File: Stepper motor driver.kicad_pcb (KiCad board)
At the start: 2 copper layers, 22 parts, among them Q1 TIP120, Q2 TIP120, Q3 TIP120, Q4 TIP120, U1 74LS175, U2 74LS157

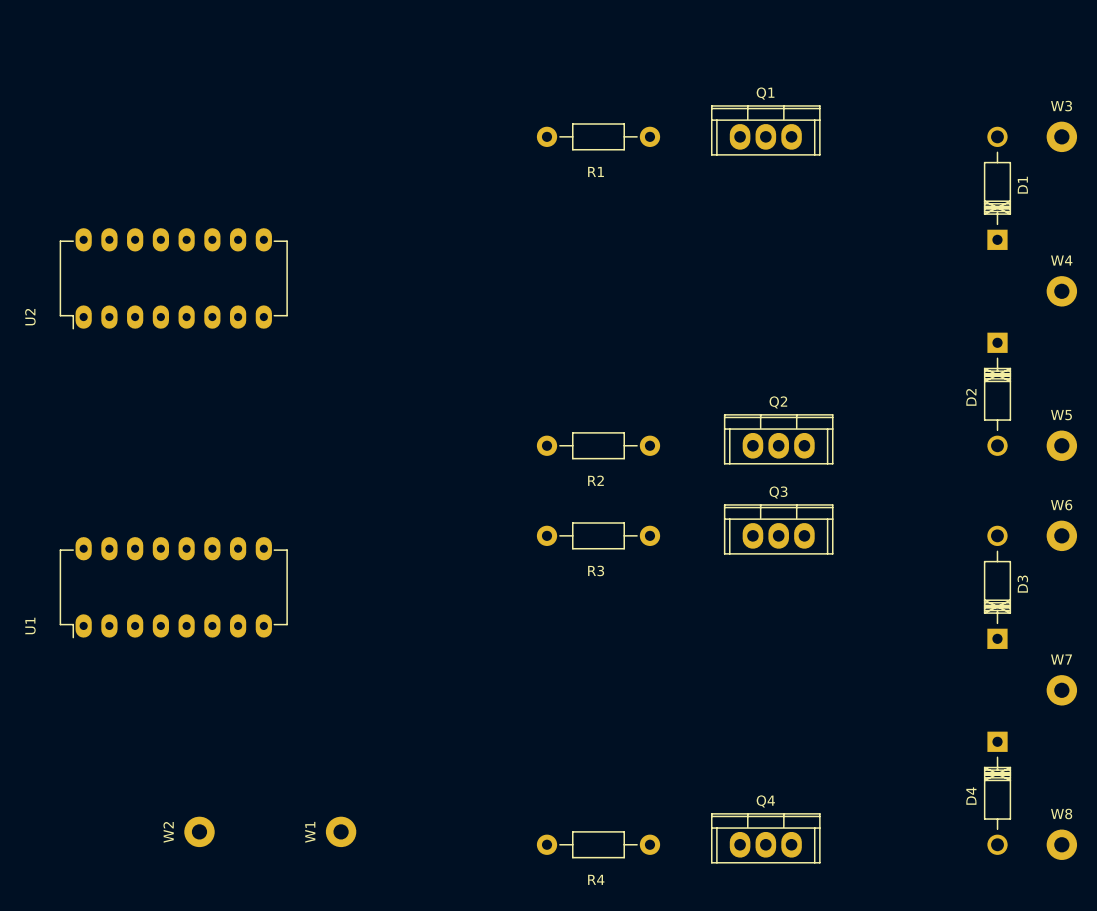
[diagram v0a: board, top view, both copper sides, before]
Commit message: finished PCB initial routing
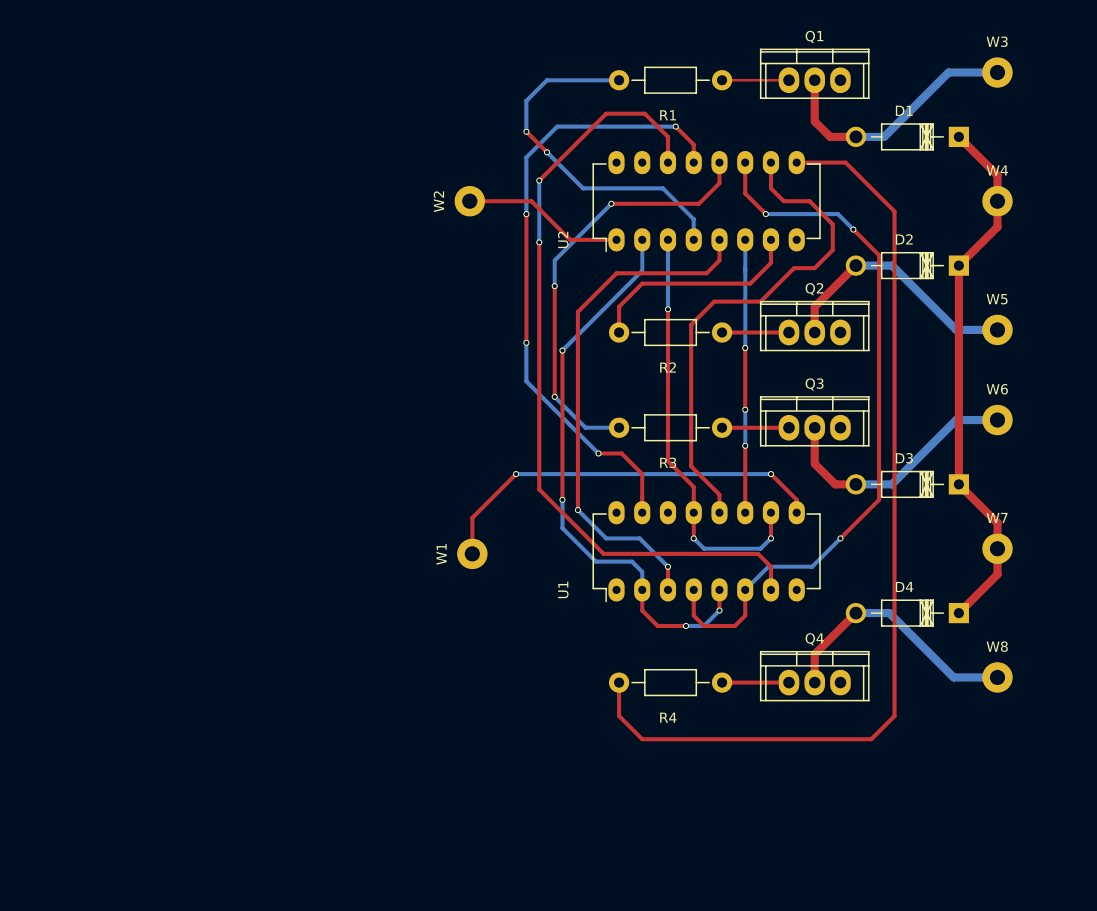
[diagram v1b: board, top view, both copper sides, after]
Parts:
- moved W2 67.7 mm to (203.2, 38.1)
- moved U2 53.1 mm to (217.7, 41.9)
- moved U1 52.7 mm to (217.7, 76.5)
- moved W1 30.3 mm to (203.5, 72.9)
- moved W8 17.7 mm to (255.3, 85.1)
- moved R4 17.5 mm to (228.1, 85.6)
- moved Q4 16.7 mm to (237.2, 85.6)
- moved D3 15.7 mm to (251.5, 66.0), turned to 180 degrees
- moved W7 15.3 mm to (255.3, 72.4)
- moved D4 13.3 mm to (251.5, 78.7), turned to 180 degrees
- moved R2 13.2 mm to (228.1, 51.1)
- moved W6 13.1 mm to (255.3, 59.7)
- moved W5 13.1 mm to (255.3, 50.8)
- moved R3 12.8 mm to (228.1, 60.5)
- moved Q2 11.7 mm to (237.2, 51.1)
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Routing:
- net Net-(R4-Pad2): track 0.00 -> 93.8 mm
- net /A1-: track 0.00 -> 77.7 mm, vias 0 -> 2
- net /A1+: track 0.00 -> 70.8 mm, vias 0 -> 3
- net /B2+: track 0.00 -> 61.4 mm, vias 0 -> 4
- net /B1+: track 0.00 -> 56.1 mm, vias 0 -> 4
- net +5V: track 0.02 -> 53.3 mm
- net /B1-: track 0.00 -> 51.2 mm, vias 0 -> 2
- net /B2-: track 0.00 -> 49.4 mm
- net Net-(R3-Pad2): track 0.00 -> 42.5 mm, vias 0 -> 3
- net /A2-: track 0.00 -> 41.5 mm, vias 0 -> 3
- net /CLK: track 0.00 -> 39.7 mm, vias 0 -> 2
- net Net-(R1-Pad2): track 0.00 -> 35.2 mm, vias 0 -> 2
- net /A2+: track 0.00 -> 27.2 mm, vias 0 -> 3
- net Net-(D1-Pad2): track 0.00 -> 25.4 mm
- net Net-(D4-Pad2): track 0.00 -> 25.1 mm
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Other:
- net class high current wire added: clearance 0.2, trace_width 0.8, via_dia 0.6, via_drill 0.4
- net class thicker wire added: clearance 0.2, trace_width 0.4, via_dia 0.6, via_drill 0.4

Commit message: fixed schematic and finished all routing
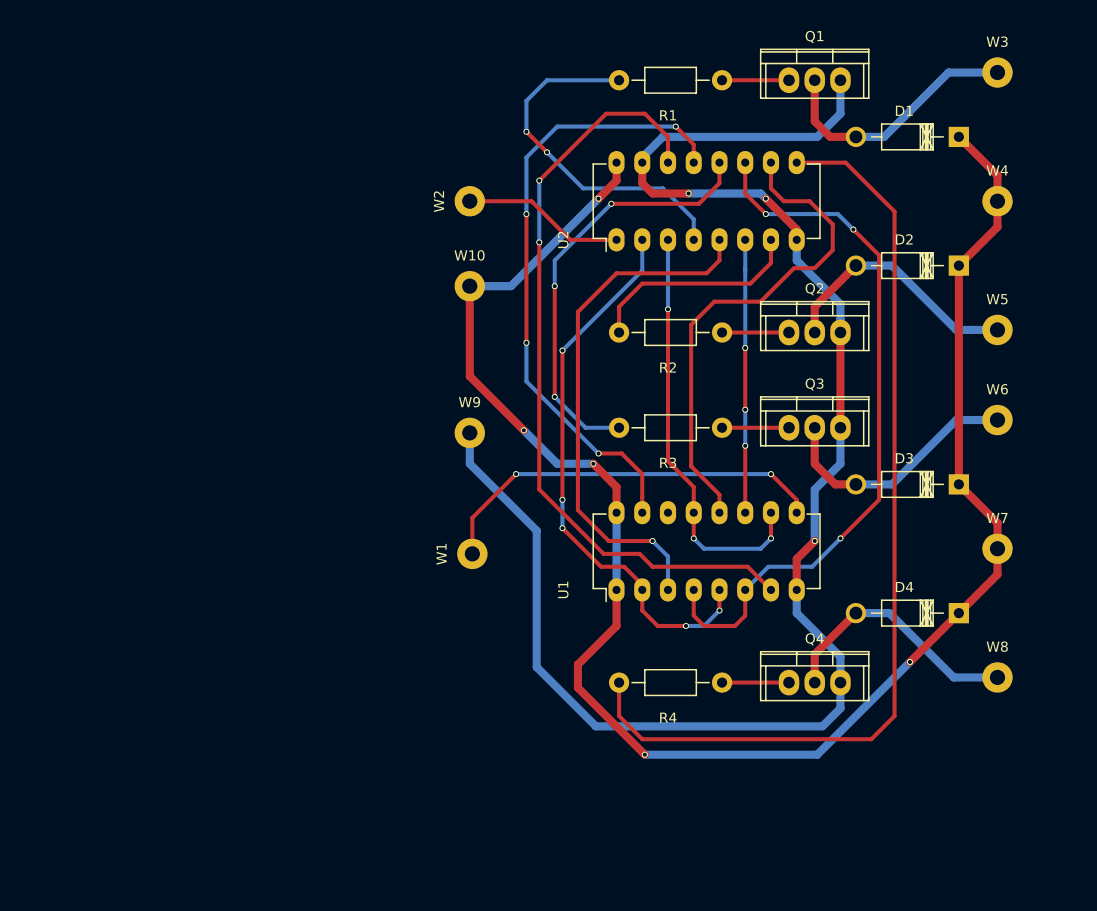
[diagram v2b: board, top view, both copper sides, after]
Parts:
- added W10: TEST_1P, Measurement_Points:Measurement_Point_Round-TH_Big, F.Cu at (203.2, 46.5)
- added W9: TEST_1P, Measurement_Points:Measurement_Point_Round-TH_Big, F.Cu at (203.2, 61.0)
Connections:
- D1 pad 1: +5V -> VCC
- D2 pad 1: +5V -> VCC
- D3 pad 1: +5V -> VCC
- D4 pad 1: +5V -> VCC
- U1 pad 1: +5V -> VCC
- W4 pad 1: +5V -> VCC
- W7 pad 1: +5V -> VCC
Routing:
- net VCC: track 0.00 -> 169.3 mm, vias 0 -> 5
- net GND: track 0.00 -> 155.9 mm, vias 0 -> 3
- net +5V: track 53.3 -> 0.00 mm
- net /A1-: track 77.7 -> 76.4 mm
- net /B1+: track 56.1 -> 55.4 mm, vias 4 -> 5
- net /B1-: track 51.2 -> 51.7 mm, vias 2 -> 1

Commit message: finished PCB completely, added gerber files and picture of layout
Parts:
- Coil 1+: renamed from W3
- Coil 1-: renamed from W5
- Coil 2+: renamed from W6
- Coil 2-: renamed from W8
- renumbered W1 to CLK, W2 to DIR, W9 to GND, W4 to VCC, W7 to VCC, W10 to VCC
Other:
- board outline added: 63 x 74.4 mm
- board text added: "Jake Vidal"
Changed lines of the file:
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@@
     (links 46)
     (no_connects 1)
-    (area 0 0 0 0)
+    (area 196.520999 20.244999 259.663001 94.817001)
     (thickness 1.6)
-    (drawings 0)
+    (drawings 7)
     (tracks 252)
     (zones 0)
@@
     (visible_elements 7FFFFFFF)
     (pcbplotparams
-      (layerselection 0x00030_80000001)
+      (layerselection 0x010f0_80000001)
       (usegerberextensions false)
-      (excludeedgelayer true)
+      (excludeedgelayer false)
       (linewidth 0.100000)
       (plotframeref false)
@@
       (psa4output false)
       (plotreference true)
-      (plotvalue true)
+      (plotvalue false)
       (plotinvisibletext false)
-      (padsonsilk false)
+      (padsonsilk true)
       (subtractmaskfromsilk false)
       (outputformat 1)
       (mirror false)
-      (drillshape 1)
+      (drillshape 0)
       (scaleselection 1)
-      (outputdirectory ""))
+      (outputdirectory ../../../))
   )
   (net 0 "")
@@
     (descr "Diode, DO-41, SOD81, Horizontal, RM 10mm,")
     (tags "Diode, DO-41, SOD81, Horizontal, RM 10mm, 1N4007, SB140,")
-    (fp_text reference D1 (at 5.38734 2.53746 180) (layer F.SilkS)
-      (effects (font (size 1 1) (thickness 0.15)))
-    )
-    (fp_text value 1N4003 (at 4.37134 -3.55854 180) (layer F.Fab)
+    (fp_text reference D1 (at 4.318 -2.286 180) (layer F.SilkS)
+      (effects (font (size 1 1) (thickness 0.15)))
+    )
+    (fp_text value 1N4003 (at 4.826 2.794 180) (layer F.Fab)
       (effects (font (size 1 1) (thickness 0.15)))
     )
@@
     (descr "Diode, DO-41, SOD81, Horizontal, RM 10mm,")
     (tags "Diode, DO-41, SOD81, Horizontal, RM 10mm, 1N4007, SB140,")
-    (fp_text reference D2 (at 5.38734 2.53746 180) (layer F.SilkS)
+    (fp_text reference D2 (at 4.318 2.286 180) (layer F.SilkS)
       (effects (font (size 1 1) (thickness 0.15)))
     )
@@
     (descr "Diode, DO-41, SOD81, Horizontal, RM 10mm,")
     (tags "Diode, DO-41, SOD81, Horizontal, RM 10mm, 1N4007, SB140,")
-    (fp_text reference D3 (at 5.38734 2.53746 180) (layer F.SilkS)
-      (effects (font (size 1 1) (thickness 0.15)))
-    )
-    (fp_text value 1N4003 (at 4.37134 -3.55854 180) (layer F.Fab)
+    (fp_text reference D3 (at 4.572 -2.286 180) (layer F.SilkS)
+      (effects (font (size 1 1) (thickness 0.15)))
+    )
+    (fp_text value 1N4003 (at 5.08 2.794 180) (layer F.Fab)
       (effects (font (size 1 1) (thickness 0.15)))
     )
@@
     (descr "Diode, DO-41, SOD81, Horizontal, RM 10mm,")
     (tags "Diode, DO-41, SOD81, Horizontal, RM 10mm, 1N4007, SB140,")
-    (fp_text reference D4 (at 5.38734 2.53746 180) (layer F.SilkS)
+    (fp_text reference D4 (at 4.572 2.286 180) (layer F.SilkS)
       (effects (font (size 1 1) (thickness 0.15)))
     )
@@
     (descr "Non Isolated JEDEC TO-220 Package")
     (tags "Power Integration YN Package")
-    (fp_text reference Q1 (at 0 -4.318) (layer F.SilkS)
+    (fp_text reference Q1 (at -4.318 2.794) (layer F.SilkS)
       (effects (font (size 1 1) (thickness 0.15)))
     )
@@
     (descr "Non Isolated JEDEC TO-220 Package")
     (tags "Power Integration YN Package")
-    (fp_text reference Q2 (at 0 -4.318) (layer F.SilkS)
+    (fp_text reference Q2 (at -3.81 2.794) (layer F.SilkS)
       (effects (font (size 1 1) (thickness 0.15)))
     )
@@
     (descr "Non Isolated JEDEC TO-220 Package")
     (tags "Power Integration YN Package")
-    (fp_text reference Q3 (at 0 -4.318) (layer F.SilkS)
+    (fp_text reference Q3 (at -3.81 -4.318) (layer F.SilkS)
       (effects (font (size 1 1) (thickness 0.15)))
     )
@@
     (descr "Non Isolated JEDEC TO-220 Package")
     (tags "Power Integration YN Package")
-    (fp_text reference Q4 (at 0 -4.318) (layer F.SilkS)
+    (fp_text reference Q4 (at -4.064 -4.318) (layer F.SilkS)
       (effects (font (size 1 1) (thickness 0.15)))
     )
@@
     (descr "Resistor, Axial,  RM 10mm, 1/3W")
     (tags "Resistor Axial RM 10mm 1/3W")
-    (fp_text reference R1 (at 5.32892 -3.50012 180) (layer F.SilkS)
+    (fp_text reference R1 (at 6.858 -2.54 180) (layer F.SilkS)
       (effects (font (size 1 1) (thickness 0.15)))
     )
@@
     (descr "Resistor, Axial,  RM 10mm, 1/3W")
     (tags "Resistor Axial RM 10mm 1/3W")
-    (fp_text reference R2 (at 5.32892 -3.50012 180) (layer F.SilkS)
+    (fp_text reference R2 (at 6.858 -2.794 180) (layer F.SilkS)
       (effects (font (size 1 1) (thickness 0.15)))
     )
@@
     (descr "Resistor, Axial,  RM 10mm, 1/3W")
     (tags "Resistor Axial RM 10mm 1/3W")
-    (fp_text reference R3 (at 5.32892 -3.50012 180) (layer F.SilkS)
+    (fp_text reference R3 (at 6.858 -2.794 180) (layer F.SilkS)
       (effects (font (size 1 1) (thickness 0.15)))
     )
@@
     (descr "Resistor, Axial,  RM 10mm, 1/3W")
     (tags "Resistor Axial RM 10mm 1/3W")
-    (fp_text reference R4 (at 5.32892 -3.50012 180) (layer F.SilkS)
-      (effects (font (size 1 1) (thickness 0.15)))
-    )
-    (fp_text value 180 (at 5.08 3.81 180) (layer F.Fab)
+    (fp_text reference R4 (at 6.858 -2.794 180) (layer F.SilkS)
+      (effects (font (size 1 1) (thickness 0.15)))
+    )
+    (fp_text value 180 (at 5.334 2.54 180) (layer F.Fab)
       (effects (font (size 1 1) (thickness 0.15)))
     )
@@
     (descr "16-lead dip package, row spacing 7.62 mm (300 mils), longer pads")
     (tags "dil dip 2.54 300")
-    (fp_text reference U1 (at 0 -5.22 90) (layer F.SilkS)
-      (effects (font (size 1 1) (thickness 0.15)))
-    )
-    (fp_text value 74LS175 (at 0 -3.72 90) (layer F.Fab)
+    (fp_text reference U1 (at 0.254 -3.556 90) (layer F.SilkS)
+      (effects (font (size 1 1) (thickness 0.15)))
+    )
+    (fp_text value 74LS175 (at 0.254 -5.334 90) (layer F.Fab)
       (effects (font (size 1 1) (thickness 0.15)))
     )
@@
     (descr "16-lead dip package, row spacing 7.62 mm (300 mils), longer pads")
     (tags "dil dip 2.54 300")
-    (fp_text reference U2 (at 0 -5.22 90) (layer F.SilkS)
-      (effects (font (size 1 1) (thickness 0.15)))
-    )
-    (fp_text value 74LS157 (at 0 -3.72 90) (layer F.Fab)
+    (fp_text reference U2 (at 4.064 -4.826 90) (layer F.SilkS)
+      (effects (font (size 1 1) (thickness 0.15)))
+    )
+    (fp_text value 74LS157 (at -1.27 -4.572 90) (layer F.Fab)
       (effects (font (size 1 1) (thickness 0.15)))
     )
@@
     (tags "Mesurement Point Round Trough Hole 3mm 1.5mm")
     (attr virtual)
-    (fp_text reference W1 (at 0 -3 90) (layer F.SilkS)
+    (fp_text reference CLK (at 0.254 -4.064 180) (layer F.SilkS)
       (effects (font (size 1 1) (thickness 0.15)))
     )
@@
     (tags "Mesurement Point Round Trough Hole 3mm 1.5mm")
     (attr virtual)
-    (fp_text reference W2 (at 0 -3 90) (layer F.SilkS)
+    (fp_text reference DIR (at 0 -4.064 180) (layer F.SilkS)
       (effects (font (size 1 1) (thickness 0.15)))
     )
@@
     (tags "Mesurement Point Round Trough Hole 3mm 1.5mm")
     (attr virtual)
-    (fp_text reference W3 (at 0 -3) (layer F.SilkS)
+    (fp_text reference "Coil 1+" (at 0.762 -3.048) (layer F.SilkS)
       (effects (font (size 1 1) (thickness 0.15)))
     )
@@
     (tags "Mesurement Point Round Trough Hole 3mm 1.5mm")
     (attr virtual)
-    (fp_text reference W4 (at 0 -3) (layer F.SilkS)
+    (fp_text reference VCC (at 0 -3) (layer F.SilkS)
       (effects (font (size 1 1) (thickness 0.15)))
     )
@@
     (tags "Mesurement Point Round Trough Hole 3mm 1.5mm")
     (attr virtual)
-    (fp_text reference W5 (at 0 -3) (layer F.SilkS)
+    (fp_text reference "Coil 1-" (at 0.762 -2.794) (layer F.SilkS)
       (effects (font (size 1 1) (thickness 0.15)))
     )
@@
     (tags "Mesurement Point Round Trough Hole 3mm 1.5mm")
     (attr virtual)
-    (fp_text reference W6 (at 0 -3) (layer F.SilkS)
+    (fp_text reference "Coil 2+" (at 0.762 -2.794) (layer F.SilkS)
       (effects (font (size 1 1) (thickness 0.15)))
     )
@@
     (tags "Mesurement Point Round Trough Hole 3mm 1.5mm")
     (attr virtual)
-    (fp_text reference W7 (at 0 -3) (layer F.SilkS)
+    (fp_text reference VCC (at 2.286 -2.54) (layer F.SilkS)
       (effects (font (size 1 1) (thickness 0.15)))
     )
@@
     (tags "Mesurement Point Round Trough Hole 3mm 1.5mm")
     (attr virtual)
-    (fp_text reference W8 (at 0 -3) (layer F.SilkS)
+    (fp_text reference "Coil 2-" (at 0.762 -2.794) (layer F.SilkS)
       (effects (font (size 1 1) (thickness 0.15)))
     )
@@
     (tags "Mesurement Point Round Trough Hole 3mm 1.5mm")
     (attr virtual)
-    (fp_text reference W9 (at 0 -3) (layer F.SilkS)
+    (fp_text reference GND (at -3.81 0) (layer F.SilkS)
       (effects (font (size 1 1) (thickness 0.15)))
     )
@@
     (tags "Mesurement Point Round Trough Hole 3mm 1.5mm")
     (attr virtual)
-    (fp_text reference W10 (at 0 -3) (layer F.SilkS)
+    (fp_text reference VCC (at -3.81 0) (layer F.SilkS)
       (effects (font (size 1 1) (thickness 0.15)))
     )
@@
       (net 23 VCC))
   )
+  (gr_text "Jake Vidal" (at 204.978 86.614 315) (layer F.SilkS)
+    (effects (font (size 1.5 1.5) (thickness 0.3)))
+  )
+  (gr_line (start 259.588 94.742) (end 259.588 20.32) (angle 90) (layer Edge.Cuts) (width 0.15))
+  (gr_line (start 205.994 94.742) (end 259.588 94.742) (angle 90) (layer Edge.Cuts) (width 0.15))
+  (gr_line (start 196.596 85.344) (end 205.994 94.742) (angle 90) (layer Edge.Cuts) (width 0.15))
+  (gr_line (start 196.596 32.766) (end 196.596 85.344) (angle 90) (layer Edge.Cuts) (width 0.15))
+  (gr_line (start 209.042 20.32) (end 196.596 32.766) (angle 90) (layer Edge.Cuts) (width 0.15))
+  (gr_line (start 259.588 20.32) (end 209.042 20.32) (angle 90) (layer Edge.Cuts) (width 0.15))
   (segment (start 241.3 31.75254) (end 244.09146 31.75254) (width 0.8) (layer B.Cu) (net 1))
   (segment (start 250.444 25.4) (end 255.27 25.4) (width 0.8) (layer B.Cu) (net 1))
